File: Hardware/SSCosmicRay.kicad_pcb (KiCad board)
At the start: 2 copper layers, 80 x 50 mm, 151 parts, among them J1 ICSP-CORTEX, J3 CONN-9, U1 MAX4477, U2 MAX4477, U3 MAX4477, U4 MAX4477, U5 MAX4477, U6 STM32L100RBT6, U7 LTC3129-SOP, U8 AOZ1280, U9 LM2903DT, X1 8MHz

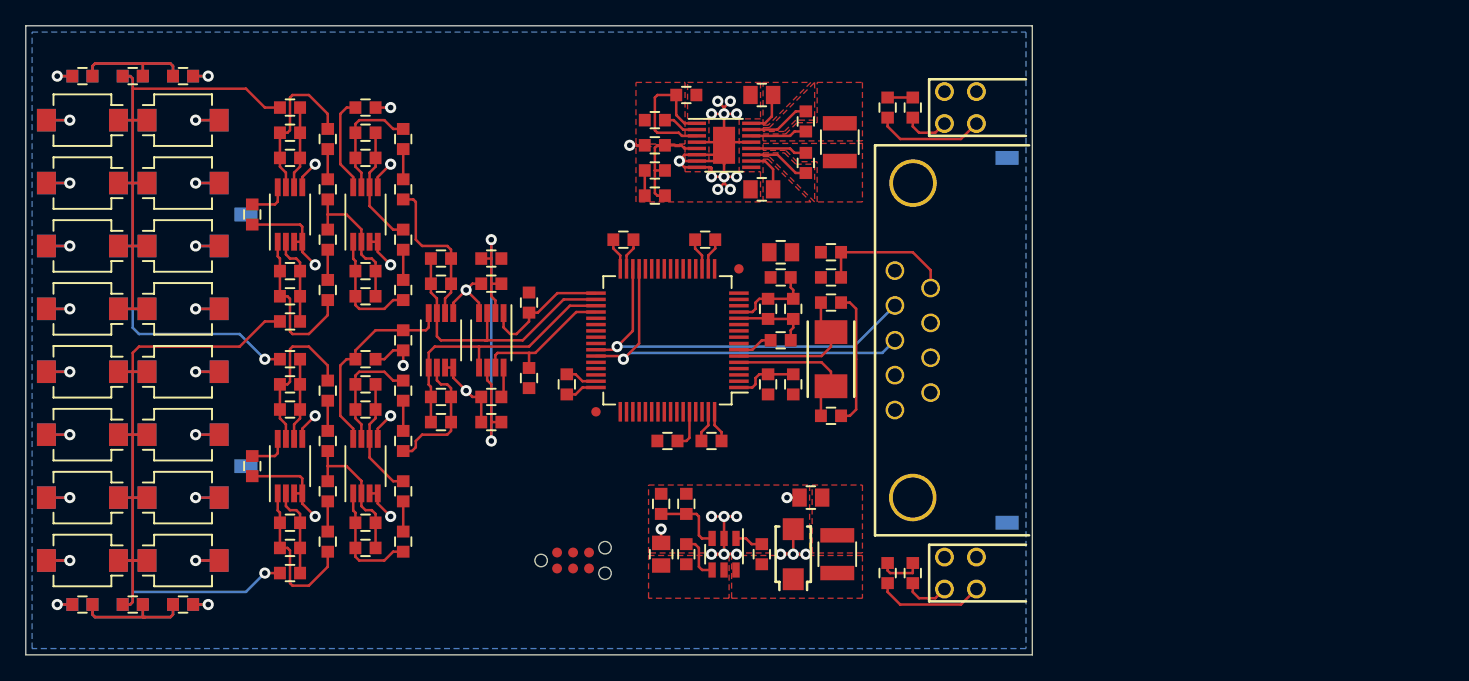
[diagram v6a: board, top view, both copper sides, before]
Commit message: Clear board, associations and annotations
Prepare for new topology
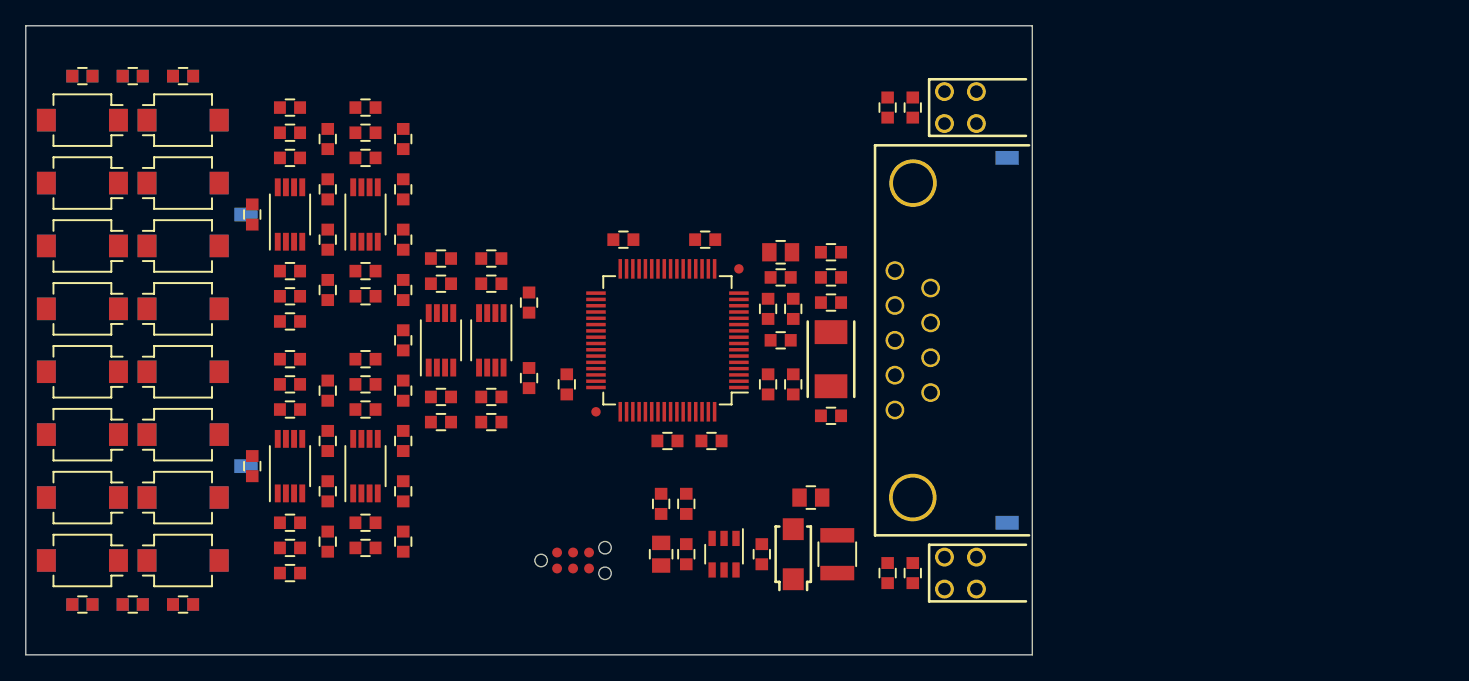
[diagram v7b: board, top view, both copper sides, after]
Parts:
- removed C36, C43: 10uF, CAPC2012-N
- removed C37: 2.2uF, CAPC1608-N
- removed C38, C40: 0.022uF, CAPC1608-N
- removed C42: 14pF, CAPC1608-N
- removed L1: 10uH, INDC3225-N
- removed R33: 10k, RESC1608-N
- removed R35: 4.7M, RESC1608-N
- removed R36: 510k, RESC1608-N
- removed U7: LTC3129-SOP, SOP50P490-17N
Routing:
- net GND: track 183.2 -> 0.00 mm, vias 53 -> 0
- net +3.3V: track 48.4 -> 0.00 mm
- net /Detector 2/Det2B: track 42.5 -> 0.00 mm, vias 1 -> 0
- net /Detector 1/Det1A: track 42.5 -> 0.00 mm
- net /Detector 2/Det2A: track 40.6 -> 0.00 mm, vias 1 -> 0
- net /Detector 1/Det1B: track 40.6 -> 0.00 mm
- net /Processor/DI: track 32.2 -> 0.00 mm, vias 1 -> 0
- net /Processor/DO: track 31.9 -> 0.00 mm, vias 1 -> 0
- net /Processor/THRSH: track 30.3 -> 0.00 mm, vias 2 -> 0
- net /Processor/A1: track 22.7 -> 0.00 mm
- net /Processor/A2: track 22.1 -> 0.00 mm
- net N-0000094: track 12.9 -> 0.00 mm
- net N-000007: track 12.9 -> 0.00 mm
- net N-0000020: track 12.8 -> 0.00 mm
- net N-00000101: track 12.8 -> 0.00 mm
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- removed copper zone on F.Cu, net +12V
- removed copper zone on F.Cu, net +3.3V
- removed copper zone on F.Cu, net /Power/BS1
- removed copper zone on F.Cu, net /Power/BS2
- removed copper zone on F.Cu, net /Power/Lx
- removed copper zone on F.Cu, net /Power/SW1
- removed copper zone on F.Cu, net /Power/SW2
- removed copper zone on F.Cu, net /Power/Vcc
- removed copper zone on B.Cu, net GND
- removed copper zone on F.Cu, net GND
- removed copper zone on F.Cu, net VCOM

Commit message: Component values
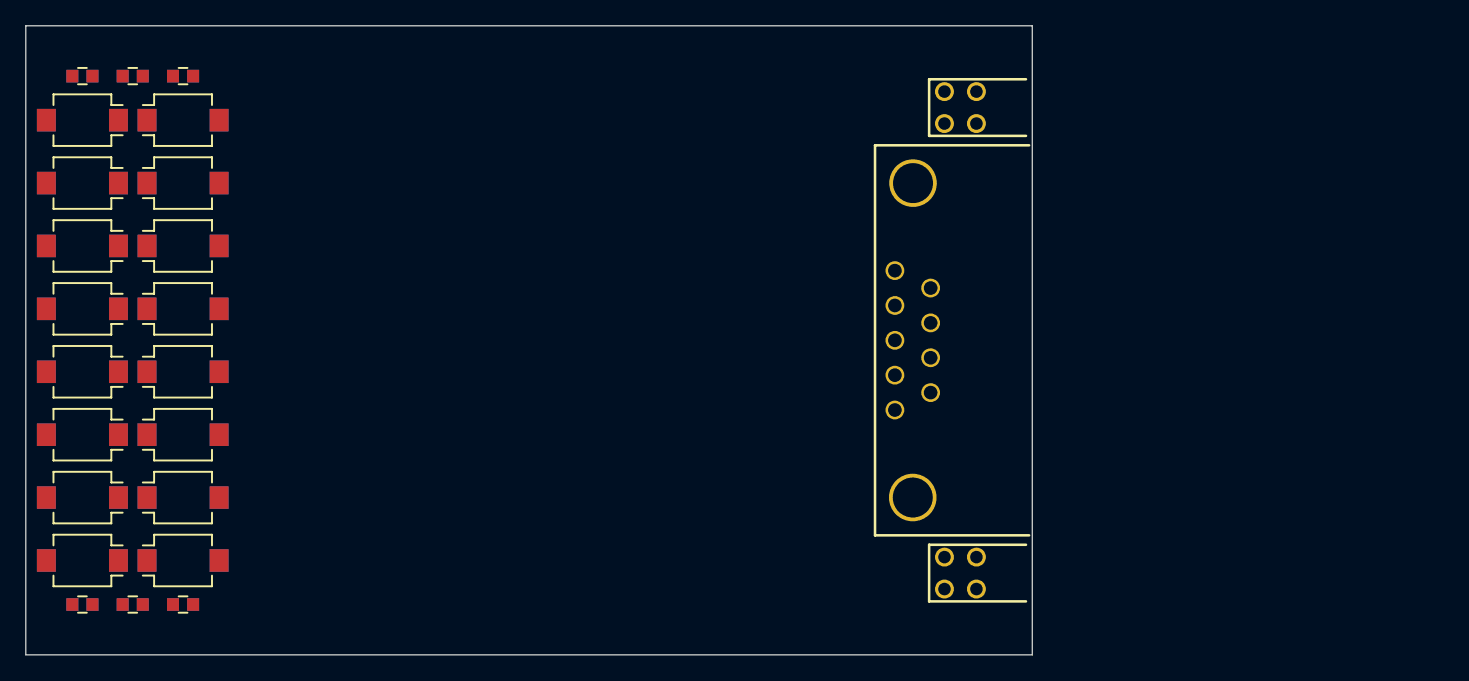
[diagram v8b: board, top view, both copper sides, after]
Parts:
- removed C10, C14, C18, C20, C21, C30, C34, C47, C49, C50, C51, C52, C53, C54, C55, C7: 0.1uF, CAPC1608-N
- removed C11, C12, C15, C24, C26, C27, C3, C31, C32, C35, C41, C5, C6: 0.01uF, CAPC1608-N
- removed C13, C2, C23, C25, C33, C4: 100pF, CAPC1608-N
- removed C16, C19: C, CAPC1608-N
- removed C17, C39, C44: 10uF, CAPC2012-N
- removed C28, C29, C8, C9: 4.7pF, CAPC1608-N
- removed C48: 1uF, CAPC1608-N
- removed D36: CDBA140, SODFL5126-N
- removed FB1: FERRITE, INDC1608-N
- removed J1: ICSP-CORTEX, CONN-TC-2030-NL
- removed L2: 10uH, INDC3225-N
- removed R10, R2, R23, R26, R30, R31, R5, R9: 1k, RESC1608-N
- removed R11, R12, R18, R19, R21, R25, R27, R32, R34, R4, R41, R42, R6: 10k, RESC1608-N
- removed R14, R15, R16, R17: 150, RESC1608-N
- removed R28, R29, R7, R8: 10M, RESC1608-N
- removed R37: 49.9k, RESC1608-N
- removed R38: 15.8k, RESC1608-N
- removed SH1, SH2, SH3, SH4: SHIELD, EMI-TE-155157X
- removed U1, U2, U3, U4, U5: MAX4477, SOP65P490-8N
- removed U6: STM32L100RBT6, QFP50P1200X1200-64N
- removed U8: AOZ1280, SOT95P280-6N
- removed U9: LM2903DT, SOP65P490-8N
- removed X1: 8MHz, XTAL-2SMD-60x35
